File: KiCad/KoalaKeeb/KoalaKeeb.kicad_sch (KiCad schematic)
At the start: 50 parts, among them J1 JLC_Battery_Con_L, Q1 IRLML2502, SW1 Switch_SW_Push, SW10 Switch_SW_Push, SW11 Switch_SW_Push, SW12 Switch_SW_Push, SW13 Switch_SW_Push, SW14 Switch_SW_Push, SW15 Switch_SW_Push, SW16 Switch_SW_Push, SW17 Switch_SW_Push, SW2 Switch_SW_Push, SW3 Switch_SW_Push, SW4 Switch_SW_Push, SW5 Switch_SW_Push, SW6 Switch_SW_Push, SW7 Switch_SW_Push, SW8 Switch_SW_Push, SW9 Switch_SW_Push, U1 Nice!Nano_L

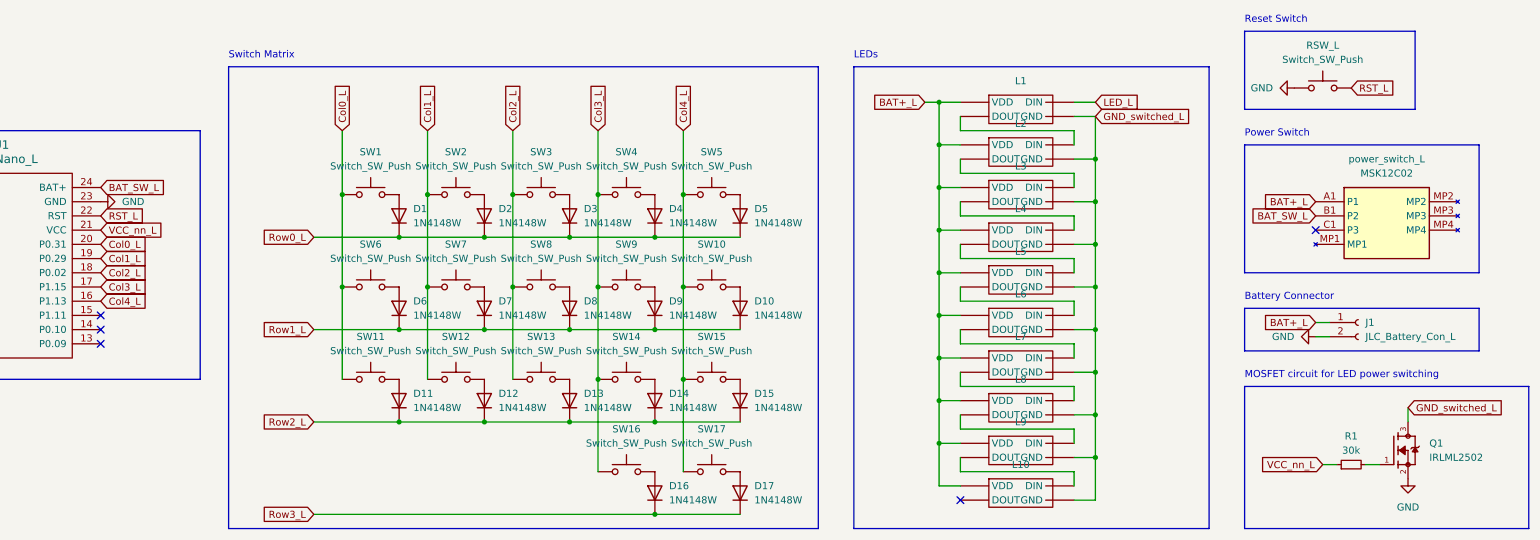
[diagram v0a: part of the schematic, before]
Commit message: remove transistor circuit
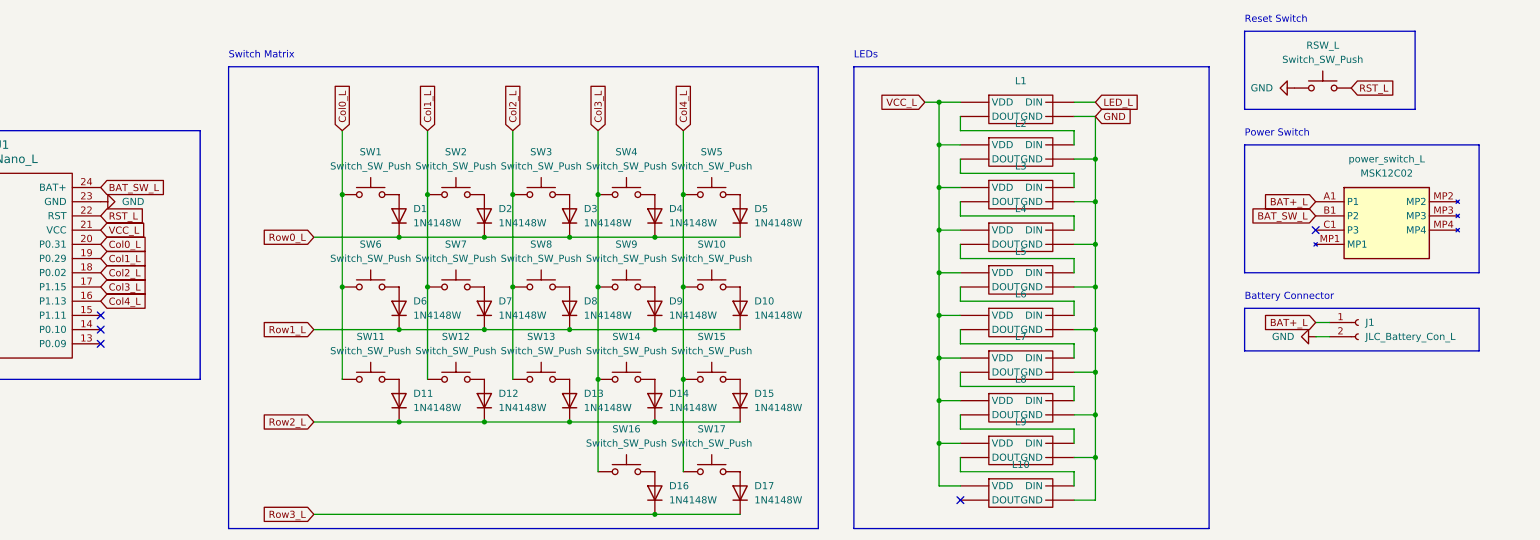
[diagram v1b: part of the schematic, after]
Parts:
- removed Q1: IRLML2502, SOT95P237X112-3N, symbol IRLML2502:IRLML2502
- removed R1: 30k, symbol Device:R_Small
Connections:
- net GND_switched_L is gone; now on net VCC_L: L1. (VDD), L10. (VDD), L2. (VDD), L3. (VDD), L4. (VDD), L5. (VDD), L6. (VDD), L7. (VDD), L8. (VDD), L9. (VDD)
- net VCC_nn_L is gone; now on net VCC_L: U1.21 (VCC)
- net BAT+_L: no longer L1. (VDD), L10. (VDD), L2. (VDD), L3. (VDD), L4. (VDD), L5. (VDD), L6. (VDD), L7. (VDD), L8. (VDD), L9. (VDD)
- net GND: now also L1. (VDD), L10. (VDD), L2. (VDD), L3. (VDD), L4. (VDD), L5. (VDD), L6. (VDD), L7. (VDD), L8. (VDD), L9. (VDD)
- net VCC_L: now reaches L10. (VDD)
- new net: L10. (VDD), L9. (VDD)
- new net: L6. (VDD), L7. (VDD)
- new net: L7. (VDD), L8. (VDD)
- new net: L4. (VDD), L5. (VDD)
- new net: L3. (VDD), L4. (VDD)
- new net: L1. (VDD), L2. (VDD)
- new net: L5. (VDD), L6. (VDD)
- new net: L2. (VDD), L3. (VDD)
- new net: L8. (VDD), L9. (VDD)
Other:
- note removed: "MOSFET circuit for LED power switching"
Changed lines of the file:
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@@
-    (stroke (width 0) (type default))
-  )
-  (wire (pts (xy 292.1 93.98) (xy 294.64 93.98))
     (stroke (width 0) (type default))
   )
@@
     (stroke (width 0) (type default))
   )
-  (wire (pts (xy 299.72 83.82) (xy 299.72 86.36))
-    (stroke (width 0) (type default))
-  )
   (wire (pts (xy 119.38 69.85) (xy 134.62 69.85))
     (stroke (width 0) (type default))
@@
     (stroke (width 0) (type default))
   )
-  (wire (pts (xy 284.48 93.98) (xy 287.02 93.98))
-    (stroke (width 0) (type default))
-  )
   (wire (pts (xy 109.22 45.72) (xy 109.22 62.23))
     (stroke (width 0) (type default))
@@
   )
   (rectangle (start 270.51 66.04) (end 312.42 73.66)
-    (stroke (width 0) (type default))
-    (fill (type none))
-  )
-  (rectangle (start 270.51 80.01) (end 321.31 105.41)
     (stroke (width 0) (type default))
     (fill (type none))
@@
   )
   (text "Power Switch" (at 270.51 35.56 0)
-    (effects (font (size 1.27 1.27)) (justify left bottom))
-  )
-  (text "MOSFET circuit for LED power switching" (at 270.51 78.74 0)
     (effects (font (size 1.27 1.27)) (justify left bottom))
   )
@@
     )
   )
-  (global_label "GND_switched_L" (shape input) (at 299.72 83.82 0) (fields_autoplaced)
-    (effects (font (size 1.27 1.27)) (justify left))
-    (property "Intersheetrefs" "${INTERSHEET_REFS}" (at 317.7033 83.82 0)
-      (effects (font (size 1.27 1.27)) (justify left) hide)
-    )
-  )
   (global_label "Row2_L" (shape input) (at 104.14 86.36 180) (fields_autoplaced)
     (effects (font (size 1.27 1.27)) (justify right))
@@
     )
   )
-  (global_label "GND_switched_L" (shape input) (at 243.84 31.75 0) (fields_autoplaced)
+  (global_label "GND" (shape input) (at 243.84 31.75 0) (fields_autoplaced)
     (effects (font (size 1.27 1.27)) (justify left))
-    (property "Intersheetrefs" "${INTERSHEET_REFS}" (at 261.8233 31.75 0)
+    (property "Intersheetrefs" "${INTERSHEET_REFS}" (at 250.6957 31.75 0)
       (effects (font (size 1.27 1.27)) (justify left) hide)
     )
@@
     )
   )
-  (global_label "VCC_nn_L" (shape input) (at 284.48 93.98 180) (fields_autoplaced)
-    (effects (font (size 1.27 1.27)) (justify right))
-    (property "Intersheetrefs" "${INTERSHEET_REFS}" (at 272.6049 93.98 0)
-      (effects (font (size 1.27 1.27)) (justify right) hide)
-    )
-  )
   (global_label "BAT_SW_L" (shape input) (at 283.21 49.53 180) (fields_autoplaced)
     (effects (font (size 1.27 1.27)) (justify right))
@@
     )
   )
-  (global_label "VCC_nn_L" (shape input) (at 66.04 52.07 0) (fields_autoplaced)
+  (global_label "VCC_L" (shape input) (at 66.04 52.07 0) (fields_autoplaced)
     (effects (font (size 1.27 1.27)) (justify left))
-    (property "Intersheetrefs" "${INTERSHEET_REFS}" (at 77.9151 52.07 0)
+    (property "Intersheetrefs" "${INTERSHEET_REFS}" (at 74.6495 52.07 0)
       (effects (font (size 1.27 1.27)) (justify left) hide)
     )
   )
-  (global_label "BAT+_L" (shape input) (at 213.36 29.21 180) (fields_autoplaced)
+  (global_label "VCC_L" (shape input) (at 213.36 29.21 180) (fields_autoplaced)
     (effects (font (size 1.27 1.27)) (justify right))
-    (property "Intersheetrefs" "${INTERSHEET_REFS}" (at 203.4805 29.21 0)
+    (property "Intersheetrefs" "${INTERSHEET_REFS}" (at 204.7505 29.21 0)
       (effects (font (size 1.27 1.27)) (justify right) hide)
     )
@@
     )
   )
-  (symbol (lib_id "power:GND") (at 299.72 96.52 0) (unit 1)
-    (in_bom yes) (on_board yes) (dnp no) (fields_autoplaced)
-    (property "Reference" "#PWR05" (at 299.72 102.87 0)
-      (effects (font (size 1.27 1.27)) hide)
-    )
-    (property "Value" "GND" (at 299.72 101.6 0)
-      (effects (font (size 1.27 1.27)))
-    )
-    (property "Footprint" "" (at 299.72 96.52 0)
-      (effects (font (size 1.27 1.27)) hide)
-    )
-    (property "Datasheet" "" (at 299.72 96.52 0)
-      (effects (font (size 1.27 1.27)) hide)
-    )
-    (pin "1")
-    (instances
-      (project "KoalaKeeb"
-        (path "/ab13a0cc-ad26-411f-843b-8e4b5c97b37f"
-          (reference "#PWR05") (unit 1)
-        )
-      )
-    )
-  )
   (symbol (lib_name "SK6812_MINI-E_1") (lib_id "KoalaKeeb-cache:SK6812_MINI-E") (at 229.87 76.2 0) (unit 1)
     (in_bom yes) (on_board yes) (dnp no) (fields_autoplaced)
@@
         )
       )
-    )
-  )
-  (symbol (lib_id "Device:R_Small") (at 289.56 93.98 90) (unit 1)
-    (in_bom yes) (on_board yes) (dnp no) (fields_autoplaced)
-    (property "Reference" "R1" (at 289.56 88.9 90)
-      (effects (font (size 1.27 1.27)))
-    )
-    (property "Value" "30k" (at 289.56 91.44 90)
-      (effects (font (size 1.27 1.27)))
-    )
-    (property "Footprint" "" (at 289.56 93.98 0)
-      (effects (font (size 1.27 1.27)) hide)
-    )
-    (property "Datasheet" "~" (at 289.56 93.98 0)
-      (effects (font (size 1.27 1.27)) hide)
-    )
-    (pin "1")
-    (pin "2")
-    (instances
-      (project "KoalaKeeb"
-        (path "/ab13a0cc-ad26-411f-843b-8e4b5c97b37f"
-          (reference "R1") (unit 1)
-        )
-      )
-    )
-  )
-  (symbol (lib_id "IRLML2502:IRLML2502") (at 297.18 91.44 0) (unit 1)
-    (in_bom yes) (on_board yes) (dnp no) (fields_autoplaced)
-    (property "Reference" "Q1" (at 303.53 90.17 0)
-      (effects (font (size 1.27 1.27)) (justify left))
-    )
-    (property "Value" "IRLML2502" (at 303.53 92.71 0)
-      (effects (font (size 1.27 1.27)) (justify left))
-    )
-    (property "Footprint" "SOT95P237X112-3N" (at 297.18 91.44 0)
-      (effects (font (size 1.27 1.27)) (justify bottom) hide)
-    )
-    (property "Datasheet" "" (at 297.18 91.44 0)
-      (effects (font (size 1.27 1.27)) hide)
-    )
-    (property "MAXIMUM_PACKAGE_HEIGHT" "1.12 mm" (at 297.18 91.44 0)
-      (effects (font (size 1.27 1.27)) (justify bottom) hide)
-    )
-    (property "STANDARD" "IPC 7351B" (at 297.18 91.44 0)
-      (effects (font (size 1.27 1.27)) (justify bottom) hide)
-    )
-    (property "PARTREV" "April 24, 2014" (at 297.18 91.44 0)
-      (effects (font (size 1.27 1.27)) (justify bottom) hide)
-    )
-    (property "SNAPEDA_PACKAGE_ID" "11907" (at 297.18 91.44 0)
-      (effects (font (size 1.27 1.27)) (justify bottom) hide)
-    )
-    (property "SNAPEDA_PN" "IRLML2502" (at 297.18 91.44 0)
-      (effects (font (size 1.27 1.27)) (justify bottom) hide)
-    )
-    (property "MANUFACTURER" "Infineon Technologies" (at 297.18 91.44 0)
-      (effects (font (size 1.27 1.27)) (justify bottom) hide)
-    )
-    (pin "1")
-    (pin "2")
-    (pin "3")
-    (instances
-      (project "KoalaKeeb"
-        (path "/ab13a0cc-ad26-411f-843b-8e4b5c97b37f"
-          (reference "Q1") (unit 1)
-        )
-      )

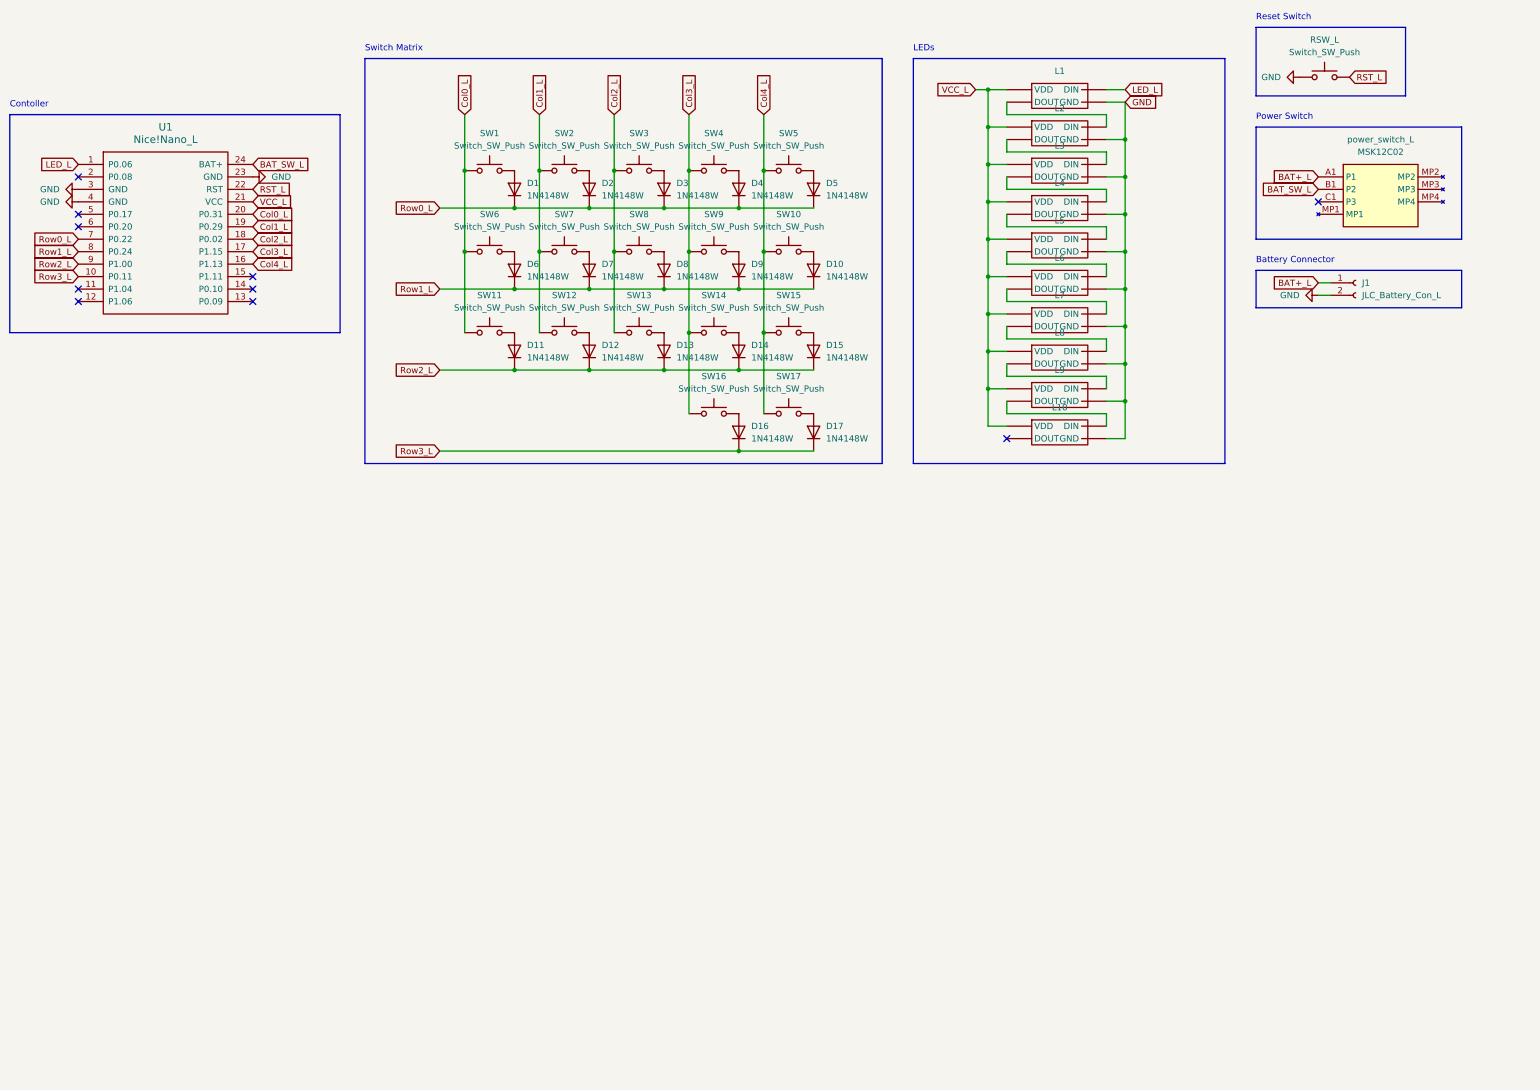
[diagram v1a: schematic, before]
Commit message: remove diodes
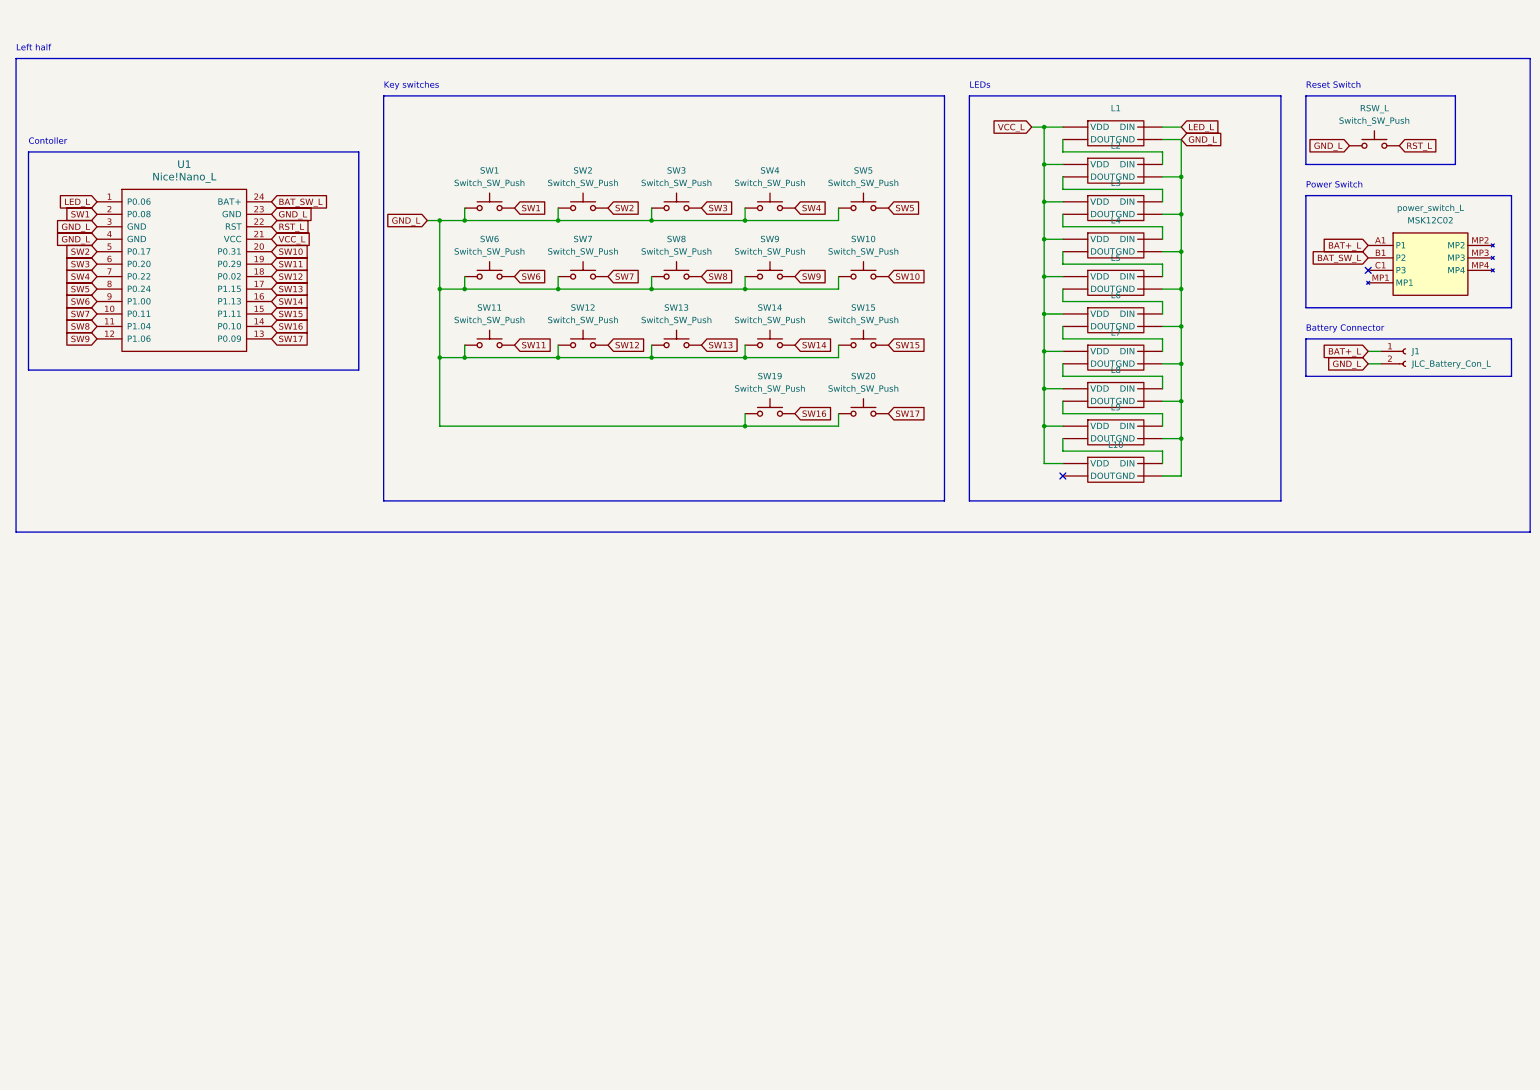
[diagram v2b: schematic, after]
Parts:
- removed D1, D10, D11, D12, D13, D14, D15, D16, D17, D2, D3, D4, D5, D6, D7, D8, D9: 1N4148W, Diode_SMD:D_SOD-123, symbol KoalaKeeb-cache:1N4148W
- removed SW16, SW17: Switch_SW_Push, symbol KoalaKeeb-cache:Switch_SW_Push
- added SW19, SW20: Switch_SW_Push, symbol KoalaKeeb-cache:Switch_SW_Push
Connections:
- net Row0_L is gone; now on net SW4: U1.7 (P0.22)
- net Row1_L is gone; now on net SW5: U1.8 (P0.24)
- net Row2_L is gone; now on net SW6: U1.9 (P1.00)
- net Row3_L is gone; now on net SW7: U1.10 (P0.11)
- net SW8: now reaches U1.11 (P1.04)
- net SW8: now also SW8.2
- net SW9: now reaches U1.12 (P1.06)
- net SW9: now also SW9.2
- net SW17: now reaches U1.13 (P0.09)
- net SW17: now also SW20.2
- net SW16: now reaches U1.14 (P0.10)
- net SW16: now also SW19.2
- net SW15: now reaches U1.15 (P1.11)
- net SW15: now also SW15.2
- net SW1: now reaches U1.2 (P0.08)
- net SW1: now also SW1.2
- net SW2: now reaches U1.5 (P0.17)
- net SW2: now also SW2.2
- net SW3: now reaches U1.6 (P0.20)
- net SW3: now also SW3.2
- net SW6: now reaches SW6.2
- net SW13: now reaches SW13.2
- net SW13: now also U1.17 (P1.15)
- net SW10: now reaches SW10.2
- net SW10: now also U1.20 (P0.31)
- net SW4: now reaches SW4.2
- net SW12: now reaches SW12.2
- net SW12: now also U1.18 (P0.02)
- net SW11: now reaches SW11.2
- net SW11: now also U1.19 (P0.29)
- net SW14: now reaches SW14.2
- net SW14: now also U1.16 (P1.13)
- net SW7: now reaches SW7.2
- net SW5: now reaches SW5.2
- net Col0_L renamed GND_L
- net GND_L: now also J1.2 (Pin_2), L1. (VDD), L10. (VDD), L2. (VDD), L3. (VDD), L4. (VDD), L5. (VDD), L6. (VDD), L7. (VDD), L8. (VDD), L9. (VDD), RSW_L.1, SW10.1, SW12.1, SW13.1, SW14.1, SW15.1, SW2.1, SW3.1, SW4.1, SW5.1, SW7.1, SW8.1, SW9.1, U1.23 (GND), U1.3 (GND), U1.4 (GND), SW19.1, SW20.1; no longer U1.20 (P0.31)
- removed net Col1_L: SW12.1, SW2.1, SW7.1, U1.19 (P0.29)
- removed net Col2_L: SW13.1, SW3.1, SW8.1, U1.18 (P0.02)
- removed net Col3_L: SW14.1, SW4.1, SW9.1, U1.17 (P1.15)
- removed net Col4_L: SW10.1, SW15.1, SW5.1, U1.16 (P1.13)
- removed net GND: J1.2 (Pin_2), L1. (VDD), L10. (VDD), L2. (VDD), L3. (VDD), L4. (VDD), L5. (VDD), L6. (VDD), L7. (VDD), L8. (VDD), L9. (VDD), RSW_L.1, U1.23 (GND), U1.3 (GND), U1.4 (GND)
- new net: L10. (VDD), L9. (VDD)
- new net: L6. (VDD), L7. (VDD)
- new net: L7. (VDD), L8. (VDD)
- new net: L4. (VDD), L5. (VDD)
- new net: L3. (VDD), L4. (VDD)
- new net: L1. (VDD), L2. (VDD)
- new net: L5. (VDD), L6. (VDD)
- new net: L2. (VDD), L3. (VDD)
- new net: L8. (VDD), L9. (VDD)
- no-connect marks 10 -> 2
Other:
- note added: "Key switches"
- note added: "Left half"
- note removed: "Switch Matrix"
- moved on the sheet: J1, L1, L10, L2, L3, L4, L5, L6, L7, L8, L9, RSW_L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
